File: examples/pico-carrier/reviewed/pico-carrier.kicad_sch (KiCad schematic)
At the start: 16 parts, among them J1 5V IN, J3 GP0-GP15, J4 GP16-GP28, PWR, U1 Pico

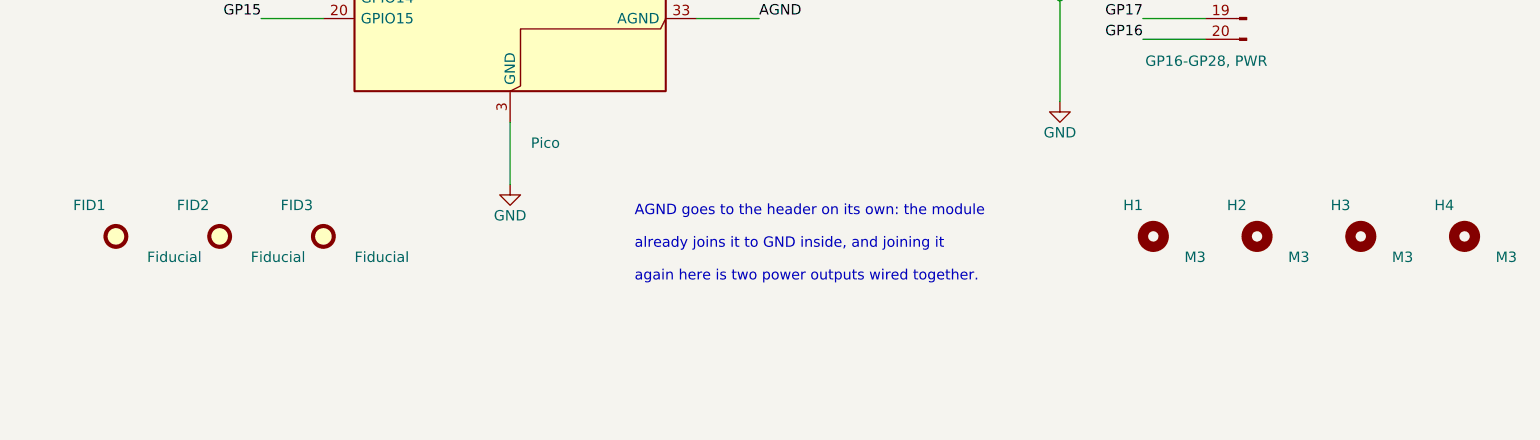
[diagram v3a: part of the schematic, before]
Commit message: Put the vias back where the copper moved, and let the fillets vote
The FPGA board came back from its re-route with two unconnected nets and
three dangling ends, and the cause was older than anything this round
added. The router hands back a via for every layer change; six passes
then reshape the copper - snapping to 45s, chamfering, spreading folds,
and now filleting - and none of them move the holes underneath. A joint
that slides a millimetre from its via is two loose ends and one broken
net, and `_unlooped` then swept the via away as orphaned, because it
kept a via only when a track ended on its exact coordinate.

Two fixes, both about what "connected" means. A via lives if kept copper
*touches* it, not if a coordinate matches. And a new `_joined` pass
re-derives the joints from the copper that actually got written: where a
net ends on two layers at one point with no via reaching it, one goes
back in. It reads the finished geometry, so it cannot drift the way six
separate passes carrying vias along with them would.

The same reasoning fixes two rules that had been measuring coordinates
rather than copper. `route.stub` matched a track end to a via's centre
exactly, and called a joint a stub whenever a reshaping pass had moved
it a quarter of a millimetre inside the very barrel it was connected to.
`route.width_step` walked a neck back to its pad and stopped at the
first width change - which, on a filleted board, is the teardrop, so
every escape's neck stopped being recognised as one.

While the three copies of the post-route pipeline were being edited for
the third time this session, they became one function. That is how
`_teardrops` had come to run on two of the three exits.

All five boards: DRC clean on both matrix versions, nothing unconnected.
Four pass their gates; the FPGA board is down to the two-layer bill it
has always had - four nets over plane cuts and one 88 degree corner.

Co-Authored-By: Claude Fable 5 <noreply@anthropic.com>
Claude-Session: https:/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
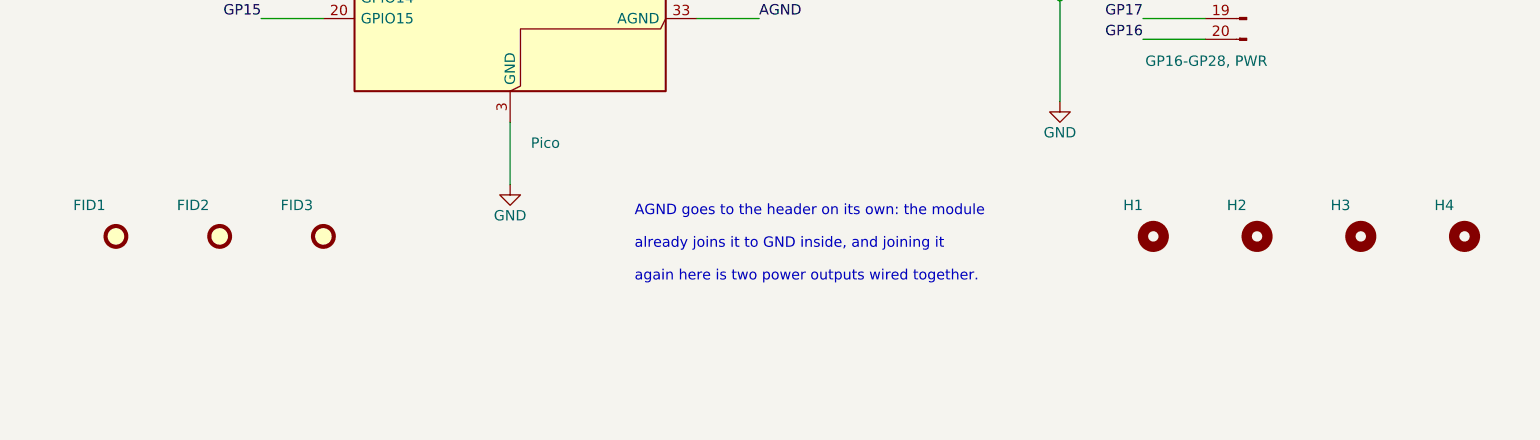
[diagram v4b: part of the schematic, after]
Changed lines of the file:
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@@
     (exclude_from_sim no) (in_bom no) (on_board yes) (dnp no)
     (property "Reference" "H1" (at 227.33 146.05 0) (effects (font (size 1.27 1.27)) (justify right)))
-    (property "Value" "M3" (at 232.41 152.4 0) (effects (font (size 1.27 1.27)) (justify left)))
+    (property "Value" "M3" (at 232.41 152.4 0) (effects (font (size 1.27 1.27)) (justify left) hide))
     (property "Footprint" "MountingHole:MountingHole_3.2mm_M3" (at 228.6 149.86 0) (effects (font (size 1.27 1.27)) hide))
     (property "Datasheet" "~" (at 228.6 149.86 0) (effects (font (size 1.27 1.27)) hide))
@@
     (exclude_from_sim no) (in_bom no) (on_board yes) (dnp no)
     (property "Reference" "H2" (at 240.03 146.05 0) (effects (font (size 1.27 1.27)) (justify right)))
-    (property "Value" "M3" (at 245.11 152.4 0) (effects (font (size 1.27 1.27)) (justify left)))
+    (property "Value" "M3" (at 245.11 152.4 0) (effects (font (size 1.27 1.27)) (justify left) hide))
     (property "Footprint" "MountingHole:MountingHole_3.2mm_M3" (at 241.29999999999998 149.86 0) (effects (font (size 1.27 1.27)) hide))
     (property "Datasheet" "~" (at 241.29999999999998 149.86 0) (effects (font (size 1.27 1.27)) hide))
@@
     (exclude_from_sim no) (in_bom no) (on_board yes) (dnp no)
     (property "Reference" "H3" (at 252.73 146.05 0) (effects (font (size 1.27 1.27)) (justify right)))
-    (property "Value" "M3" (at 257.81 152.4 0) (effects (font (size 1.27 1.27)) (justify left)))
+    (property "Value" "M3" (at 257.81 152.4 0) (effects (font (size 1.27 1.27)) (justify left) hide))
     (property "Footprint" "MountingHole:MountingHole_3.2mm_M3" (at 254.0 149.86 0) (effects (font (size 1.27 1.27)) hide))
     (property "Datasheet" "~" (at 254.0 149.86 0) (effects (font (size 1.27 1.27)) hide))
@@
     (exclude_from_sim no) (in_bom no) (on_board yes) (dnp no)
     (property "Reference" "H4" (at 265.43 146.05 0) (effects (font (size 1.27 1.27)) (justify right)))
-    (property "Value" "M3" (at 270.51 152.4 0) (effects (font (size 1.27 1.27)) (justify left)))
+    (property "Value" "M3" (at 270.51 152.4 0) (effects (font (size 1.27 1.27)) (justify left) hide))
     (property "Footprint" "MountingHole:MountingHole_3.2mm_M3" (at 266.7 149.86 0) (effects (font (size 1.27 1.27)) hide))
     (property "Datasheet" "~" (at 266.7 149.86 0) (effects (font (size 1.27 1.27)) hide))
@@
     (exclude_from_sim no) (in_bom no) (on_board yes) (dnp no)
     (property "Reference" "FID1" (at 100.33 146.05 0) (effects (font (size 1.27 1.27)) (justify right)))
-    (property "Value" "Fiducial" (at 105.41 152.4 0) (effects (font (size 1.27 1.27)) (justify left)))
+    (property "Value" "Fiducial" (at 105.41 152.4 0) (effects (font (size 1.27 1.27)) (justify left) hide))
     (property "Footprint" "Fiducial:Fiducial_1mm_Mask2mm" (at 101.6 149.86 0) (effects (font (size 1.27 1.27)) hide))
     (property "Datasheet" "~" (at 101.6 149.86 0) (effects (font (size 1.27 1.27)) hide))
@@
     (exclude_from_sim no) (in_bom no) (on_board yes) (dnp no)
     (property "Reference" "FID2" (at 113.03 146.05 0) (effects (font (size 1.27 1.27)) (justify right)))
-    (property "Value" "Fiducial" (at 118.11 152.4 0) (effects (font (size 1.27 1.27)) (justify left)))
+    (property "Value" "Fiducial" (at 118.11 152.4 0) (effects (font (size 1.27 1.27)) (justify left) hide))
     (property "Footprint" "Fiducial:Fiducial_1mm_Mask2mm" (at 114.3 149.86 0) (effects (font (size 1.27 1.27)) hide))
     (property "Datasheet" "~" (at 114.3 149.86 0) (effects (font (size 1.27 1.27)) hide))
@@
     (exclude_from_sim no) (in_bom no) (on_board yes) (dnp no)
     (property "Reference" "FID3" (at 125.73 146.05 0) (effects (font (size 1.27 1.27)) (justify right)))
-    (property "Value" "Fiducial" (at 130.81 152.4 0) (effects (font (size 1.27 1.27)) (justify left)))
+    (property "Value" "Fiducial" (at 130.81 152.4 0) (effects (font (size 1.27 1.27)) (justify left) hide))
     (property "Footprint" "Fiducial:Fiducial_1mm_Mask2mm" (at 127.0 149.86 0) (effects (font (size 1.27 1.27)) hide))
     (property "Datasheet" "~" (at 127.0 149.86 0) (effects (font (size 1.27 1.27)) hide))

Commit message: Leave room for the screw, and print the ink where the board is
The screw holes were placed against the hole's own courtyard, which is the
drill plus a whisker - so on four of the five boards a hole sat inside a
connector's mating space, closest 0.42 mm. What goes through an M3 hole is a
pan head on a washer, seven millimetres of steel lying flat, and a connector
wants its shell, its wires and the fingers that fit them on top of that. The
spot search now keeps the fastener's own circle clear of every part body and
gives connectors CONNECTOR_ACCESS more, and three rules say so when a board
does not: mechanical.fastener_clearance, mechanical.connector_access and
mechanical.fastener_copper, all blocking for a generated design.

Silk was measured with a per-character advance of 0.78, and KiCad's stroke
font is proportional at 0.94 to 1.07. Everything downstream of that estimate
was placing ink where it did not fit: a legend across a capacitor's land, a
designator through the board's own name. `_text_extent` takes the top of the
measured range, adds the fab's clearance and is used by every silk placement.

Three placements also fell through to a position nobody chose. A designator
that found nothing kept its library offset, which for a part in a corner
points off the board; the board id took the first of eight fixed strips; a
legend took the least bad of six spots. All three are scored now, over
candidate sets wide enough to have an answer - and a pad-less footprint, which
is what a mounting hole is, is no longer skipped outright.

silk.off_board reports the case KiCad's own test cannot: ink that clears the
edge entirely is never printed, and DRC only measures ink that crosses it.

_unspiked redraws a corner tighter than a right angle as the elbow between its
neighbours - one diagonal, one straight, no step back to a heading the line
has already left. It is never longer than what it replaces.

All four fast boards: 0 errors, 0 warnings.

Co-Authored-By: Claude Fable 5 <no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
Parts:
- removed FID3: Fiducial, Fiducial:Fiducial_1mm_Mask2mm, symbol Mechanical:Fiducial
- removed H2, H3, H4: M3, MountingHole:MountingHole_3.2mm_M3, symbol Mechanical:MountingHole
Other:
- moved on the sheet: FID1, FID2, H1
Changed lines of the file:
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@@
     (instances (project "pico-carrier" (path "/f86b03a2-2f64-5dc5-a6a7-b575bc25ae3a" (reference "D3") (unit 1))))
   )
-  (symbol (lib_id "Mechanical:MountingHole") (at 228.6 149.86 0.0) (unit 1)
+  (symbol (lib_id "Mechanical:MountingHole") (at 101.6 149.86 0.0) (unit 1)
     (exclude_from_sim no) (in_bom no) (on_board yes) (dnp no)
-    (property "Reference" "H1" (at 227.33 146.05 0) (effects (font (size 1.27 1.27)) (justify right)))
-    (property "Value" "M3" (at 232.41 152.4 0) (effects (font (size 1.27 1.27)) (justify left) hide))
-    (property "Footprint" "MountingHole:MountingHole_3.2mm_M3" (at 228.6 149.86 0) (effects (font (size 1.27 1.27)) hide))
-    (property "Datasheet" "~" (at 228.6 149.86 0) (effects (font (size 1.27 1.27)) hide))
-    (property "MPN" "n/a" (at 228.6 149.86 0) (effects (font (size 1.27 1.27)) hide))
-    (property "Manufacturer" "n/a" (at 228.6 149.86 0) (effects (font (size 1.27 1.27)) hide))
-    (instances (project "pico-carrier" (path "/f86b03a2-2f64-5dc5-a6a7-b575bc25ae3a" (reference "H1") (unit 1))))
-  )
-  (symbol (lib_id "Mechanical:MountingHole") (at 241.29999999999998 149.86 0.0) (unit 1)
-    (exclude_from_sim no) (in_bom no) (on_board yes) (dnp no)
-    (property "Reference" "H2" (at 240.03 146.05 0) (effects (font (size 1.27 1.27)) (justify right)))
-    (property "Value" "M3" (at 245.11 152.4 0) (effects (font (size 1.27 1.27)) (justify left) hide))
-    (property "Footprint" "MountingHole:MountingHole_3.2mm_M3" (at 241.29999999999998 149.86 0) (effects (font (size 1.27 1.27)) hide))
-    (property "Datasheet" "~" (at 241.29999999999998 149.86 0) (effects (font (size 1.27 1.27)) hide))
-    (property "MPN" "n/a" (at 241.29999999999998 149.86 0) (effects (font (size 1.27 1.27)) hide))
-    (property "Manufacturer" "n/a" (at 241.29999999999998 149.86 0) (effects (font (size 1.27 1.27)) hide))
-    (instances (project "pico-carrier" (path "/f86b03a2-2f64-5dc5-a6a7-b575bc25ae3a" (reference "H2") (unit 1))))
-  )
-  (symbol (lib_id "Mechanical:MountingHole") (at 254.0 149.86 0.0) (unit 1)
-    (exclude_from_sim no) (in_bom no) (on_board yes) (dnp no)
-    (property "Reference" "H3" (at 252.73 146.05 0) (effects (font (size 1.27 1.27)) (justify right)))
-    (property "Value" "M3" (at 257.81 152.4 0) (effects (font (size 1.27 1.27)) (justify left) hide))
-    (property "Footprint" "MountingHole:MountingHole_3.2mm_M3" (at 254.0 149.86 0) (effects (font (size 1.27 1.27)) hide))
-    (property "Datasheet" "~" (at 254.0 149.86 0) (effects (font (size 1.27 1.27)) hide))
-    (property "MPN" "n/a" (at 254.0 149.86 0) (effects (font (size 1.27 1.27)) hide))
-    (property "Manufacturer" "n/a" (at 254.0 149.86 0) (effects (font (size 1.27 1.27)) hide))
-    (instances (project "pico-carrier" (path "/f86b03a2-2f64-5dc5-a6a7-b575bc25ae3a" (reference "H3") (unit 1))))
-  )
-  (symbol (lib_id "Mechanical:MountingHole") (at 266.7 149.86 0.0) (unit 1)
-    (exclude_from_sim no) (in_bom no) (on_board yes) (dnp no)
-    (property "Reference" "H4" (at 265.43 146.05 0) (effects (font (size 1.27 1.27)) (justify right)))
-    (property "Value" "M3" (at 270.51 152.4 0) (effects (font (size 1.27 1.27)) (justify left) hide))
-    (property "Footprint" "MountingHole:MountingHole_3.2mm_M3" (at 266.7 149.86 0) (effects (font (size 1.27 1.27)) hide))
-    (property "Datasheet" "~" (at 266.7 149.86 0) (effects (font (size 1.27 1.27)) hide))
-    (property "MPN" "n/a" (at 266.7 149.86 0) (effects (font (size 1.27 1.27)) hide))
-    (property "Manufacturer" "n/a" (at 266.7 149.86 0) (effects (font (size 1.27 1.27)) hide))
-    (instances (project "pico-carrier" (path "/f86b03a2-2f64-5dc5-a6a7-b575bc25ae3a" (reference "H4") (unit 1))))
-  )
-  (symbol (lib_id "Mechanical:Fiducial") (at 101.6 149.86 0.0) (unit 1)
-    (exclude_from_sim no) (in_bom no) (on_board yes) (dnp no)
-    (property "Reference" "FID1" (at 100.33 146.05 0) (effects (font (size 1.27 1.27)) (justify right)))
-    (property "Value" "Fiducial" (at 105.41 152.4 0) (effects (font (size 1.27 1.27)) (justify left) hide))
-    (property "Footprint" "Fiducial:Fiducial_1mm_Mask2mm" (at 101.6 149.86 0) (effects (font (size 1.27 1.27)) hide))
+    (property "Reference" "H1" (at 100.33 146.05 0) (effects (font (size 1.27 1.27)) (justify right)))
+    (property "Value" "M3" (at 105.41 152.4 0) (effects (font (size 1.27 1.27)) (justify left) hide))
+    (property "Footprint" "MountingHole:MountingHole_3.2mm_M3" (at 101.6 149.86 0) (effects (font (size 1.27 1.27)) hide))
     (property "Datasheet" "~" (at 101.6 149.86 0) (effects (font (size 1.27 1.27)) hide))
     (property "MPN" "n/a" (at 101.6 149.86 0) (effects (font (size 1.27 1.27)) hide))
     (property "Manufacturer" "n/a" (at 101.6 149.86 0) (effects (font (size 1.27 1.27)) hide))
-    (instances (project "pico-carrier" (path "/f86b03a2-2f64-5dc5-a6a7-b575bc25ae3a" (reference "FID1") (unit 1))))
+    (instances (project "pico-carrier" (path "/f86b03a2-2f64-5dc5-a6a7-b575bc25ae3a" (reference "H1") (unit 1))))
   )
   (symbol (lib_id "Mechanical:Fiducial") (at 114.3 149.86 0.0) (unit 1)
     (exclude_from_sim no) (in_bom no) (on_board yes) (dnp no)
-    (property "Reference" "FID2" (at 113.03 146.05 0) (effects (font (size 1.27 1.27)) (justify right)))
+    (property "Reference" "FID1" (at 113.03 146.05 0) (effects (font (size 1.27 1.27)) (justify right)))
     (property "Value" "Fiducial" (at 118.11 152.4 0) (effects (font (size 1.27 1.27)) (justify left) hide))
     (property "Footprint" "Fiducial:Fiducial_1mm_Mask2mm" (at 114.3 149.86 0) (effects (font (size 1.27 1.27)) hide))
@@
     (property "MPN" "n/a" (at 114.3 149.86 0) (effects (font (size 1.27 1.27)) hide))
     (property "Manufacturer" "n/a" (at 114.3 149.86 0) (effects (font (size 1.27 1.27)) hide))
-    (instances (project "pico-carrier" (path "/f86b03a2-2f64-5dc5-a6a7-b575bc25ae3a" (reference "FID2") (unit 1))))
+    (instances (project "pico-carrier" (path "/f86b03a2-2f64-5dc5-a6a7-b575bc25ae3a" (reference "FID1") (unit 1))))
   )
   (symbol (lib_id "Mechanical:Fiducial") (at 127.0 149.86 0.0) (unit 1)
     (exclude_from_sim no) (in_bom no) (on_board yes) (dnp no)
-    (property "Reference" "FID3" (at 125.73 146.05 0) (effects (font (size 1.27 1.27)) (justify right)))
+    (property "Reference" "FID2" (at 125.73 146.05 0) (effects (font (size 1.27 1.27)) (justify right)))
     (property "Value" "Fiducial" (at 130.81 152.4 0) (effects (font (size 1.27 1.27)) (justify left) hide))
     (property "Footprint" "Fiducial:Fiducial_1mm_Mask2mm" (at 127.0 149.86 0) (effects (font (size 1.27 1.27)) hide))
@@
     (property "MPN" "n/a" (at 127.0 149.86 0) (effects (font (size 1.27 1.27)) hide))
     (property "Manufacturer" "n/a" (at 127.0 149.86 0) (effects (font (size 1.27 1.27)) hide))
-    (instances (project "pico-carrier" (path "/f86b03a2-2f64-5dc5-a6a7-b575bc25ae3a" (reference "FID3") (unit 1))))
+    (instances (project "pico-carrier" (path "/f86b03a2-2f64-5dc5-a6a7-b575bc25ae3a" (reference "FID2") (unit 1))))
   )
   (wire (pts (xy 180.34 107.95) (xy 180.34 105.41)) (stroke (width 0) (type default)))
